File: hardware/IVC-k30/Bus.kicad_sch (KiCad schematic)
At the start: 1 part, among them U4 VME64-P1-5R-NS

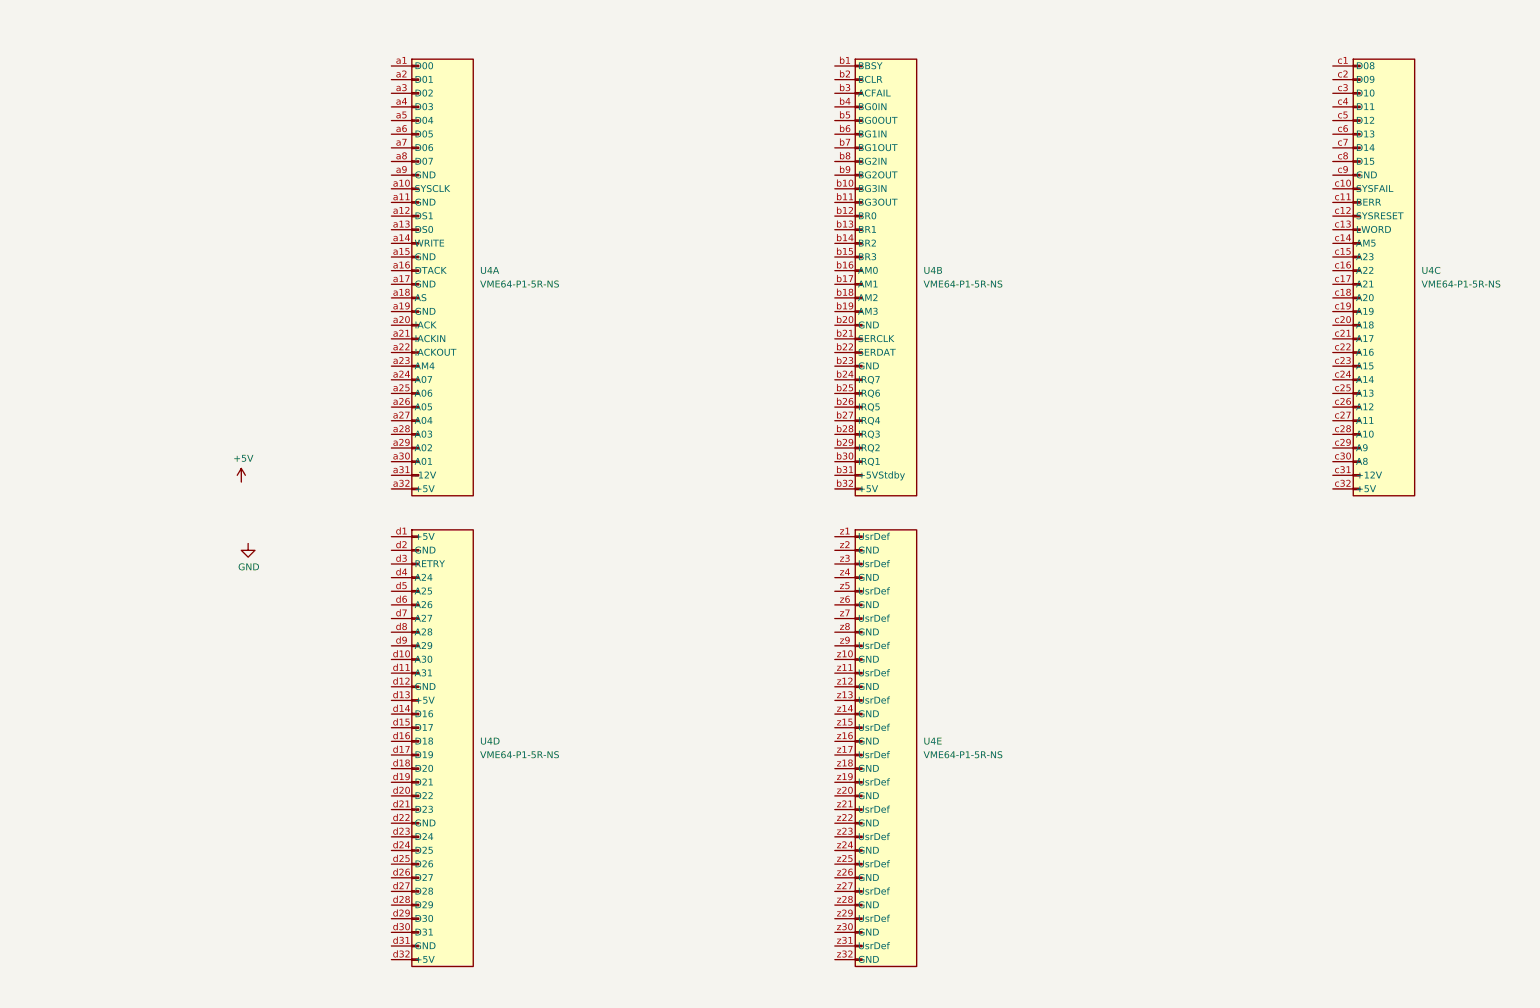
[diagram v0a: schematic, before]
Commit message: Updated k30 CPU card
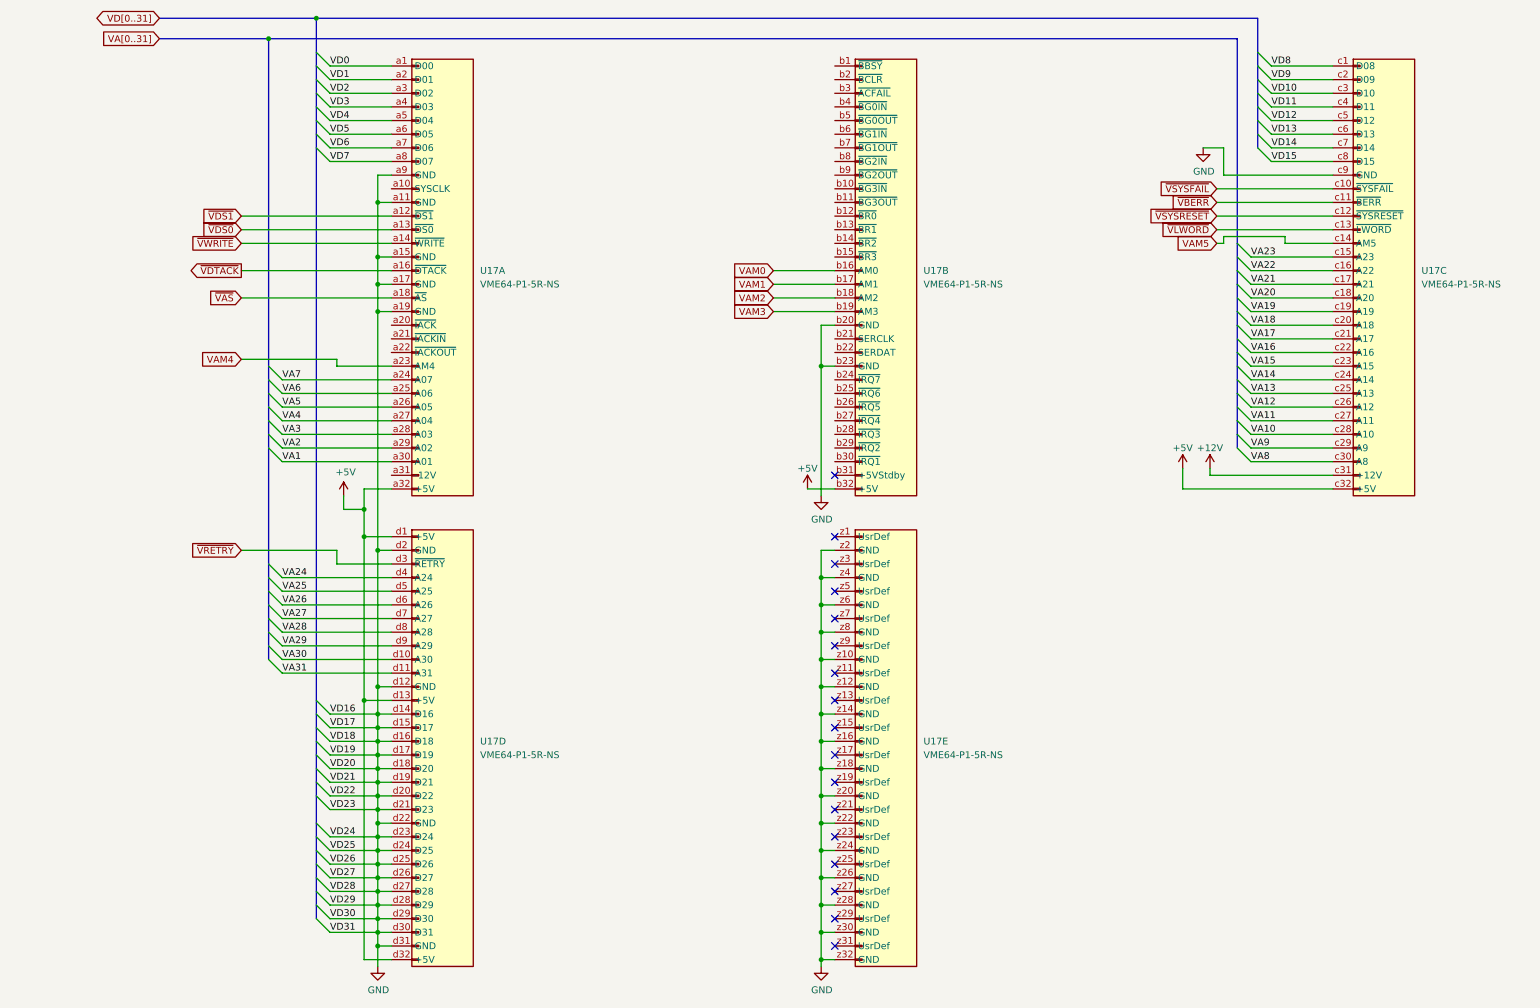
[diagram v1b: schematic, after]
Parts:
- renumbered U4 to U17
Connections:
- net +5V: now also U17.a32 (+5V), U17.b32 (+5V), U17.c32 (+5V), U17.d1 (+5V), U17.d13 (+5V), U17.d32 (+5V)
- net GND: now also U17.a11 (GND), U17.a15 (GND), U17.a17 (GND), U17.a19 (GND), U17.a9 (GND), U17.b20 (GND), U17.b23 (GND), U17.c9 (GND), U17.d12 (GND), U17.d14 (D16), U17.d15 (D17), U17.d16 (D18), U17.d17 (D19), U17.d18 (D20), U17.d19 (D21), U17.d2 (GND), U17.d20 (D22), U17.d21 (D23), U17.d22 (GND), U17.d23 (D24), U17.d24 (D25), U17.d25 (D26), U17.d26 (D27), U17.d27 (D28), U17.d28 (D29), U17.d29 (D30), U17.d30 (D31), U17.d31 (GND), U17.z10 (GND), U17.z12 (GND), U17.z14 (GND), U17.z16 (GND), U17.z18 (GND), U17.z2 (GND), U17.z20 (GND), U17.z22 (GND), U17.z24 (GND), U17.z26 (GND), U17.z28 (GND), U17.z30 (GND), U17.z32 (GND), U17.z4 (GND), U17.z6 (GND), U17.z8 (GND)
- net VA30: now reaches U17.d10 (A30)
- net VA31: now reaches U17.d11 (A31)
- net ~{VRETRY}: now reaches U17.d3 (~{RETRY})
- net VA24: now reaches U17.d4 (A24)
- net VA25: now reaches U17.d5 (A25)
- net VA26: now reaches U17.d6 (A26)
- net VA27: now reaches U17.d7 (A27)
- net VA28: now reaches U17.d8 (A28)
- net VA29: now reaches U17.d9 (A29)
- net VAM0: now reaches U17.b16 (AM0)
- net VAM1: now reaches U17.b17 (AM1)
- net VAM2: now reaches U17.b18 (AM2)
- net VAM3: now reaches U17.b19 (AM3)
- net VD8: now reaches U17.c1 (D08)
- net ~{VSYSFAIL}: now reaches U17.c10 (~{SYSFAIL})
- net ~{VBERR}: now reaches U17.c11 (~{BERR})
- net ~{VSYSRESET}: now reaches U17.c12 (~{SYSRESET})
- net ~{VLWORD}: now reaches U17.c13 (~{LWORD})
- net VAM5: now reaches U17.c14 (AM5)
- net VA23: now reaches U17.c15 (A23)
- net VA22: now reaches U17.c16 (A22)
- net VA21: now reaches U17.c17 (A21)
- net VA20: now reaches U17.c18 (A20)
- net VA19: now reaches U17.c19 (A19)
- net VD9: now reaches U17.c2 (D09)
- net VA18: now reaches U17.c20 (A18)
- net VA17: now reaches U17.c21 (A17)
- net VA16: now reaches U17.c22 (A16)
- net VA15: now reaches U17.c23 (A15)
- net VA14: now reaches U17.c24 (A14)
- net VA13: now reaches U17.c25 (A13)
- net VA12: now reaches U17.c26 (A12)
- net VA11: now reaches U17.c27 (A11)
- net VA10: now reaches U17.c28 (A10)
- net VA9: now reaches U17.c29 (A9)
- net VD10: now reaches U17.c3 (D10)
- net VA8: now reaches U17.c30 (A8)
- net +12V: now reaches U17.c31 (+12V)
- net VD11: now reaches U17.c4 (D11)
- net VD12: now reaches U17.c5 (D12)
- net VD13: now reaches U17.c6 (D13)
- net VD14: now reaches U17.c7 (D14)
- net VD15: now reaches U17.c8 (D15)
- net VD0: now reaches U17.a1 (D00)
- net ~{VDS1}: now reaches U17.a12 (~{DS1})
- net ~{VDS0}: now reaches U17.a13 (~{DS0})
- net ~{VWRITE}: now reaches U17.a14 (~{WRITE})
- net ~{VDTACK}: now reaches U17.a16 (~{DTACK})
- net ~{VAS}: now reaches U17.a18 (~{AS})
- net VD1: now reaches U17.a2 (D01)
- net VAM4: now reaches U17.a23 (AM4)
- net VA7: now reaches U17.a24 (A07)
- net VA6: now reaches U17.a25 (A06)
- net VA5: now reaches U17.a26 (A05)
- net VA4: now reaches U17.a27 (A04)
- net VA3: now reaches U17.a28 (A03)
- net VA2: now reaches U17.a29 (A02)
- net VD2: now reaches U17.a3 (D02)
- net VA1: now reaches U17.a30 (A01)
- net VD3: now reaches U17.a4 (D03)
- net VD4: now reaches U17.a5 (D04)
- net VD5: now reaches U17.a6 (D05)
- net VD6: now reaches U17.a7 (D06)
- net VD7: now reaches U17.a8 (D07)
- no-connect marks 0 -> 17
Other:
- moved on the sheet: U17A, U17B, U17C

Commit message: Committed changes to k30 board from Oct 9th 2023
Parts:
- added U18: 74LS148, symbol 74xx:74LS148
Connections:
- net +5V: now also U17.d12 (GND); no longer U17.d13 (+5V)
- net GND: now also U17.d13 (+5V); no longer U17.d12 (GND), U17.d14 (D16), U17.d15 (D17), U17.d16 (D18), U17.d17 (D19), U17.d18 (D20), U17.d19 (D21), U17.d20 (D22), U17.d21 (D23), U17.d23 (D24), U17.d24 (D25), U17.d25 (D26), U17.d26 (D27), U17.d27 (D28), U17.d28 (D29), U17.d29 (D30), U17.d30 (D31)
- net ~{VBBSY}: now reaches U17.b1 (~{BBSY})
- net ~{VBCLR}: now reaches U17.b2 (~{BCLR})
- net ~{VACFAIL}: now reaches U17.b3 (~{ACFAIL})
- net VSYSCLK: now reaches U17.a10 (SYSCLK)
- new net VD16: U17.d14 (D16)
- new net VD17: U17.d15 (D17)
- new net VD18: U17.d16 (D18)
- new net VD19: U17.d17 (D19)
- new net VD20: U17.d18 (D20)
- new net VD21: U17.d19 (D21)
- new net VD22: U17.d20 (D22)
- new net VD23: U17.d21 (D23)
- new net VD24: U17.d23 (D24)
- new net VD25: U17.d24 (D25)
- new net VD26: U17.d25 (D26)
- new net VD27: U17.d26 (D27)
- new net VD28: U17.d27 (D28)
- new net VD29: U17.d28 (D29)
- new net VD30: U17.d29 (D30)
- new net VD31: U17.d30 (D31)
- no-connect marks 17 -> 20
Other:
- note added: "TODO: how will interrupts work? Should you have a priority encoder on the IRQ lines?"
- note added: "TODO: need some kind of selector, to select one of the bus arbitration levels this board should request with"
